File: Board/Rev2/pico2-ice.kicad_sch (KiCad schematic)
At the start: 124 parts, among them J1 USB_C_Receptacle_USB2.0, J2 Conn_02x20_Odd_Even, J3 Conn_02x20_Odd_Even, J5 BM03B-SRSS-TB, J6 SFV22R-2STE1HLF, SW1 CS1213AGF260, SW2 CS1213AGF260, U1 NCP115AMX120TCG, U2 W25Q32JVSSIQ, U3 RP2350_80QFN, U4 TL431DBZ, U5 APS6404L-3SQN-SN, U6 ICE40UP5K-SG48ITR, U8 W25Q32JVSSIQ, U9 NCP115AMX330TCG, Y1 ABM8-272-T3

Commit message: updated design and output files
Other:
- moved on the sheet: C28, C31, C33, C34, D1, R11, SJ4

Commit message: output files
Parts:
- J6: ${REFERENCE} (none) -> ${REFERENCE}
- LOGO1: footprint CUSTOM:tinyAI_logo -> logo1:tiny_13X5_new
- LOGO4: value OSHW ID: US002140 -> OSHW ID: US002372
- U3: MPN (none) -> RP2350B; Manufacturer (none) -> Raspberry Pi
- U4: MPN (none) -> TL431BQDBZR; Manufacturer (none) -> Texas Instruments
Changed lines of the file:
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@@
 			)
 		)
+		(property "${REFERENCE}" "${REFERENCE}"
+			(at 233.68 214.63 0)
+			(effects
+				(font
+					(size 1.27 1.27)
+				)
+				(hide yes)
+			)
+		)
 		(pin "17"
 		)
@@
 			)
 		)
-		(property "Footprint" "CUSTOM:tinyAI_logo"
+		(property "Footprint" "logo1:tiny_13X5_new"
 			(at 421.64 391.16 0)
 			(effects
@@
 			)
 		)
+		(property "Manufacturer" "Texas Instruments"
+			(at 191.77 307.34 90)
+			(effects
+				(font
+					(size 1.27 1.27)
+				)
+				(hide yes)
+			)
+		)
+		(property "MPN" "TL431BQDBZR"
+			(at 191.77 307.34 90)
+			(effects
+				(font
+					(size 1.27 1.27)
+				)
+				(hide yes)
+			)
+		)
 		(pin "2"
 		)
@@
 			)
 		)
-		(property "Description" ""
+		(property "Description" "QFN-80-EP(10x10) Microcontrollers (MCU/MPU/SOC) ROHS"
+			(at 109.22 200.66 0)
+			(effects
+				(font
+					(size 1.27 1.27)
+				)
+				(hide yes)
+			)
+		)
+		(property "MPN" "RP2350B "
+			(at 109.22 200.66 0)
+			(effects
+				(font
+					(size 1.27 1.27)
+				)
+				(hide yes)
+			)
+		)
+		(property "Manufacturer" "Raspberry Pi "
 			(at 109.22 200.66 0)
 			(effects
@@
 			)
 		)
-		(property "Value" "OSHW ID: US002140"
+		(property "Value" "OSHW ID: US002372"
 			(at 397.51 388.7724 0)
 			(effects

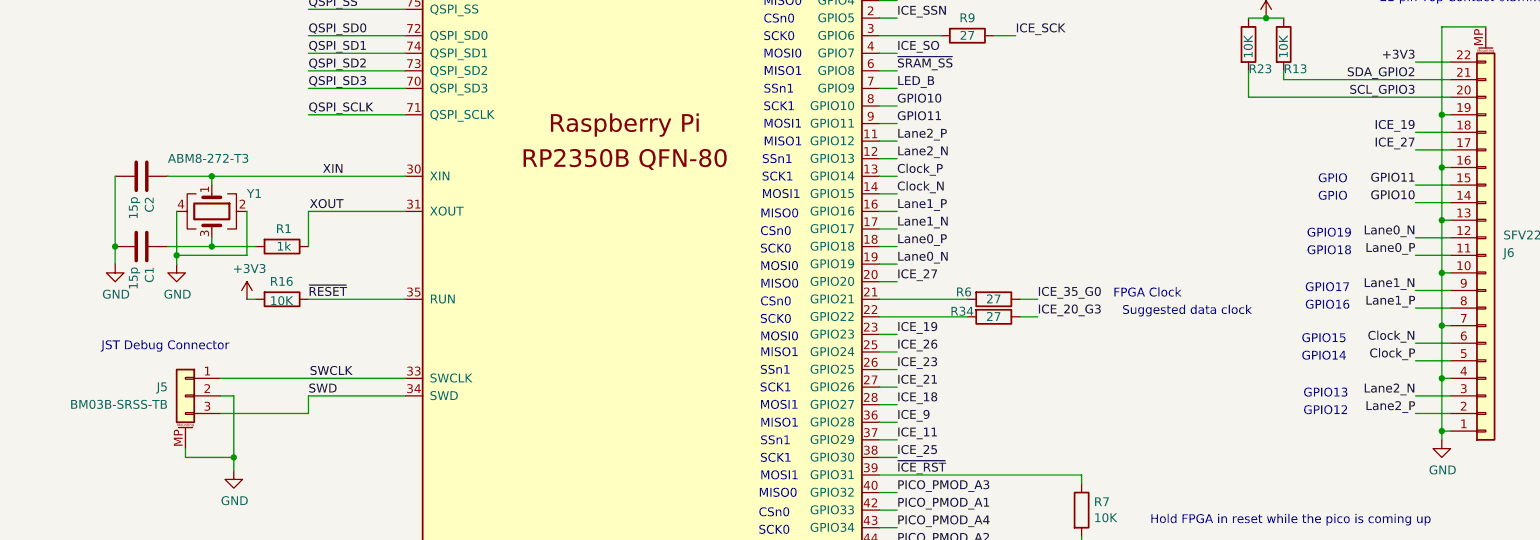
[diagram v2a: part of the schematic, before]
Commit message: Changed loading caps to 10pF, changed HSTX port naming to be consistent with other RPi boards with no routing changes, added docs for FPC connector
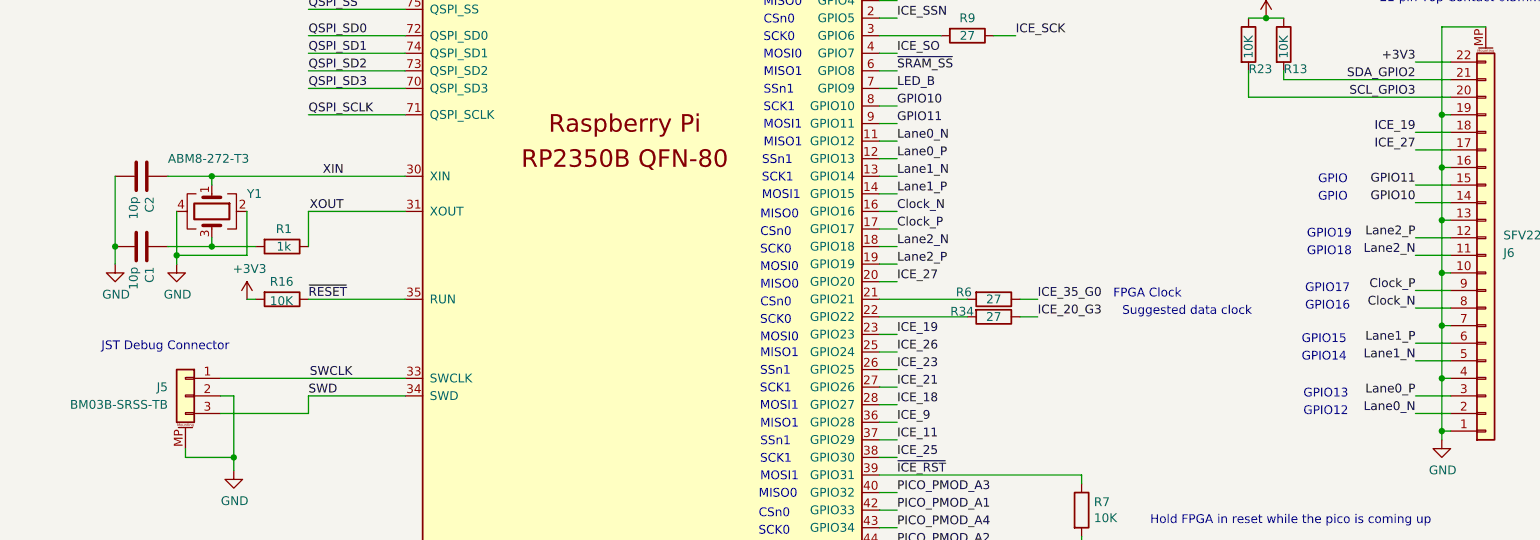
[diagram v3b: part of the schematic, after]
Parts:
- C1, C2: value 15p -> 10p; MPN GRM1555C1E150JA01D -> GRM1555C1E100JA01D
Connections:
- net Clock_N: now also J6.8 (Pin_8), U3.16 (GPIO16); no longer J6.6 (Pin_6), U3.14 (GPIO15)
- net Clock_P: now also J6.9 (Pin_9), U3.17 (GPIO17); no longer J6.5 (Pin_5), U3.13 (GPIO14)
- net Lane0_N: now also J6.2 (Pin_2), U3.11 (GPIO12); no longer J6.12 (Pin_12), U3.19 (GPIO19)
- net Lane0_P: now also J6.3 (Pin_3), U3.12 (GPIO13); no longer J6.11 (Pin_11), U3.18 (GPIO18)
- net Lane1_N: now also J6.5 (Pin_5), U3.13 (GPIO14); no longer J6.9 (Pin_9), U3.17 (GPIO17)
- net Lane1_P: now also J6.6 (Pin_6), U3.14 (GPIO15); no longer J6.8 (Pin_8), U3.16 (GPIO16)
- net Lane2_N: now also J6.11 (Pin_11), U3.18 (GPIO18); no longer J6.3 (Pin_3), U3.12 (GPIO13)
- net Lane2_P: now also J6.12 (Pin_12), U3.19 (GPIO19); no longer J6.2 (Pin_2), U3.11 (GPIO12)
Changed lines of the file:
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@@
 		)
 	)
-	(label "ICE_SO"
-		(at 513.715 41.91 0)
+	(label "Lane0_P"
+		(at 223.52 234.95 180)
 		(effects
 			(font
 				(size 1.27 1.27)
 			)
-			(justify left bottom)
+			(justify right bottom)
 		)
 	)
-	(label "ICE_35_G0"
-		(at 168.91 220.98 0)
+	(label "Lane2_P"
+		(at 223.52 212.09 180)
+		(effects
+			(font
+				(size 1.27 1.27)
+			)
+			(justify right bottom)
+		)
+	)
+	(label "ICE_SO"
+		(at 513.715 41.91 0)
 		(effects
 			(font
@@
 		)
 	)
-	(label "Lane1_N"
-		(at 148.59 210.82 0)
+	(label "ICE_35_G0"
+		(at 168.91 220.98 0)
 		(effects
 			(font
@@
 		)
 	)
-	(label "Lane1_N"
-		(at 223.52 219.71 180)
-		(effects
-			(font
-				(size 1.27 1.27)
-			)
-			(justify right bottom)
-		)
-	)
 	(label "ADC7"
 		(at 421.64 90.17 180)
@@
 		)
 	)
+	(label "Lane2_N"
+		(at 223.52 214.63 180)
+		(effects
+			(font
+				(size 1.27 1.27)
+			)
+			(justify right bottom)
+		)
+	)
 	(label "QSPI_SCLK"
 		(at 55.88 393.7 180)
@@
 		)
 	)
-	(label "Lane1_P"
-		(at 148.59 208.28 0)
-		(effects
-			(font
-				(size 1.27 1.27)
-			)
-			(justify left bottom)
-		)
-	)
 	(label "~{ICE_RST}"
 		(at 536.575 179.07 180)
@@
 		)
 	)
-	(label "Lane1_P"
-		(at 223.52 222.25 180)
-		(effects
-			(font
-				(size 1.27 1.27)
-			)
-			(justify right bottom)
-		)
-	)
 	(label "PICO_PMOD_B4"
 		(at 513.715 77.47 0)
@@
 		)
 	)
-	(label "Lane0_N"
-		(at 148.59 215.9 0)
-		(effects
-			(font
-				(size 1.27 1.27)
-			)
-			(justify left bottom)
-		)
-	)
 	(label "PICO_PMOD_B2"
 		(at 148.59 266.7 0)
@@
 		)
 	)
-	(label "ICE_35_G0"
-		(at 435.61 208.28 180)
+	(label "Lane2_N"
+		(at 148.59 213.36 0)
 		(effects
 			(font
 				(size 1.27 1.27)
 			)
-			(justify right bottom)
+			(justify left bottom)
 		)
 	)
-	(label "PICO_PMOD_B3"
-		(at 148.59 259.08 0)
+	(label "ICE_35_G0"
+		(at 435.61 208.28 180)
 		(effects
 			(font
 				(size 1.27 1.27)
 			)
-			(justify left bottom)
+			(justify right bottom)
 		)
 	)
-	(label "Lane2_P"
-		(at 223.52 237.49 180)
+	(label "PICO_PMOD_B3"
+		(at 148.59 259.08 0)
 		(effects
 			(font
 				(size 1.27 1.27)
 			)
-			(justify right bottom)
+			(justify left bottom)
 		)
 	)
@@
 		)
 	)
+	(label "Lane0_P"
+		(at 148.59 200.66 0)
+		(effects
+			(font
+				(size 1.27 1.27)
+			)
+			(justify left bottom)
+		)
+	)
+	(label "Lane1_P"
+		(at 148.59 205.74 0)
+		(effects
+			(font
+				(size 1.27 1.27)
+			)
+			(justify left bottom)
+		)
+	)
 	(label "ADC4"
 		(at 148.59 281.94 0)
@@
 		)
 	)
-	(label "Clock_P"
-		(at 223.52 229.87 180)
-		(effects
-			(font
-				(size 1.27 1.27)
-			)
-			(justify right bottom)
-		)
-	)
 	(label "ICE_19"
 		(at 493.395 49.53 180)
@@
 		)
 	)
-	(label "PICO_PMOD_A3"
-		(at 148.59 248.92 0)
+	(label "Lane1_N"
+		(at 148.59 203.2 0)
 		(effects
 			(font
@@
 		)
 	)
-	(label "Clock_N"
-		(at 223.52 227.33 180)
+	(label "PICO_PMOD_A3"
+		(at 148.59 248.92 0)
 		(effects
 			(font
 				(size 1.27 1.27)
 			)
-			(justify right bottom)
+			(justify left bottom)
 		)
 	)
@@
 		)
 	)
+	(label "Clock_N"
+		(at 223.52 222.25 180)
+		(effects
+			(font
+				(size 1.27 1.27)
+			)
+			(justify right bottom)
+		)
+	)
 	(label "ICE_32"
 		(at 435.61 200.66 180)
@@
 		)
 	)
-	(label "Lane0_P"
-		(at 223.52 214.63 180)
-		(effects
-			(font
-				(size 1.27 1.27)
-			)
-			(justify right bottom)
-		)
-	)
 	(label "ADC2|PB"
 		(at 148.59 276.86 0)
@@
 		)
 	)
-	(label "Lane0_P"
-		(at 148.59 213.36 0)
-		(effects
-			(font
-				(size 1.27 1.27)
-			)
-			(justify left bottom)
-		)
-	)
 	(label "ICE_SSN"
 		(at 493.395 41.91 180)
@@
 		)
 	)
-	(label "Clock_P"
-		(at 148.59 203.2 0)
-		(effects
-			(font
-				(size 1.27 1.27)
-			)
-			(justify left bottom)
-		)
-	)
 	(label "ICE_12|IO2"
 		(at 421.64 41.91 180)
@@
 		)
 	)
-	(label "ICE_35_G0"
-		(at 447.04 62.23 0)
+	(label "Lane1_P"
+		(at 223.52 227.33 180)
 		(effects
 			(font
 				(size 1.27 1.27)
 			)
-			(justify left bottom)
+			(justify right bottom)
 		)
 	)
-	(label "Lane0_N"
-		(at 223.52 212.09 180)
+	(label "ICE_35_G0"
+		(at 447.04 62.23 0)
 		(effects
 			(font
 				(size 1.27 1.27)
 			)
-			(justify right bottom)
+			(justify left bottom)
 		)
 	)
@@
 		)
 	)
-	(label "Lane2_P"
-		(at 148.59 198.12 0)
-		(effects
-			(font
-				(size 1.27 1.27)
-			)
-			(justify left bottom)
-		)
-	)
 	(label "USB_D-"
 		(at 172.72 160.02 0)
@@
 		)
 	)
+	(label "Clock_N"
+		(at 148.59 208.28 0)
+		(effects
+			(font
+				(size 1.27 1.27)
+			)
+			(justify left bottom)
+		)
+	)
 	(label "ICE_43"
 		(at 435.61 213.36 180)
@@
 		)
 	)
+	(label "Clock_P"
+		(at 223.52 219.71 180)
+		(effects
+			(font
+				(size 1.27 1.27)
+			)
+			(justify right bottom)
+		)
+	)
 	(label "QSPI_SD2"
 		(at 100.33 393.7 180)
@@
 		)
 	)
+	(label "Lane0_N"
+		(at 148.59 198.12 0)
+		(effects
+			(font
+				(size 1.27 1.27)
+			)
+			(justify left bottom)
+		)
+	)
 	(label "ICE_18"
 		(at 148.59 236.22 0)
@@
 		)
 	)
-	(label "Lane2_N"
-		(at 148.59 200.66 0)
+	(label "Lane2_P"
+		(at 148.59 215.9 0)
 		(effects
 			(font
@@
 		)
 	)
-	(label "Lane2_N"
-		(at 223.52 234.95 180)
-		(effects
-			(font
-				(size 1.27 1.27)
-			)
-			(justify right bottom)
-		)
-	)
 	(label "~{USB_BOOT}"
 		(at 181.61 369.57 180)
@@
 		)
 	)
+	(label "Lane0_N"
+		(at 223.52 237.49 180)
+		(effects
+			(font
+				(size 1.27 1.27)
+			)
+			(justify right bottom)
+		)
+	)
 	(label "ADC4"
 		(at 514.35 87.63 0)
@@
 		)
 	)
+	(label "Clock_P"
+		(at 148.59 210.82 0)
+		(effects
+			(font
+				(size 1.27 1.27)
+			)
+			(justify left bottom)
+		)
+	)
 	(label "ADC2|PB"
 		(at 494.03 67.31 180)
@@
 		)
 	)
-	(label "Clock_N"
-		(at 148.59 205.74 0)
-		(effects
-			(font
-				(size 1.27 1.27)
-			)
-			(justify left bottom)
-		)
-	)
 	(label "ICE_LED_R"
 		(at 429.006 226.06 0)
@@
 		)
 	)
+	(label "Lane1_N"
+		(at 223.52 229.87 180)
+		(effects
+			(font
+				(size 1.27 1.27)
+			)
+			(justify right bottom)
+		)
+	)
 	(label "ICE_LED_B"
 		(at 514.35 67.31 0)
@@
 			)
 		)
-		(property "Value" "15p"
+		(property "Value" "10p"
 			(at 38.227 206.121 0)
 			(effects
@@
 			)
 		)
-		(property "Description" "CAP CER 15PF 25V COG 0402"
+		(property "Description" "CAP CER 10PF 25V COG 0402"
 			(at 39.37 203.2 0)
 			(effects
@@
 			)
 		)
-		(property "MPN" "GRM1555C1E150JA01D"
+		(property "MPN" "GRM1555C1E100JA01D"
 			(at 39.37 203.2 0)
 			(effects
@@
 			)
 		)
-		(property "Value" "15p"
+		(property "Value" "10p"
 			(at 38.227 216.281 0)
 			(effects
@@
 			)
 		)
-		(property "Description" "CAP CER 15PF 25V COG 0402"
+		(property "Description" "CAP CER 10PF 25V COG 0402"
 			(at 39.37 213.36 0)
 			(effects
@@
 			)
 		)
-		(property "MPN" "GRM1555C1E150JA01D"
+		(property "MPN" "GRM1555C1E100JA01D"
 			(at 39.37 213.36 0)
 			(effects
